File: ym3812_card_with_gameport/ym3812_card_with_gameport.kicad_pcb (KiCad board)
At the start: 2 copper layers, 115.6 x 106.7 mm, 79 parts, among them IC1 74LS138, IC11 NE558, IC12 74HCT02, IC13 74LS74, IC18 74LS244, IC2 74LS138, IC3 74LS138, IC4 74LS245, IC6 YM3812, IC7 Y3014B, IC8 LM324, IC9 TDA7233, J1 Bus_ISA_8bit, J2 Conn_02x04_Odd_Even, J3 Conn_02x03_Counter_Clockwise

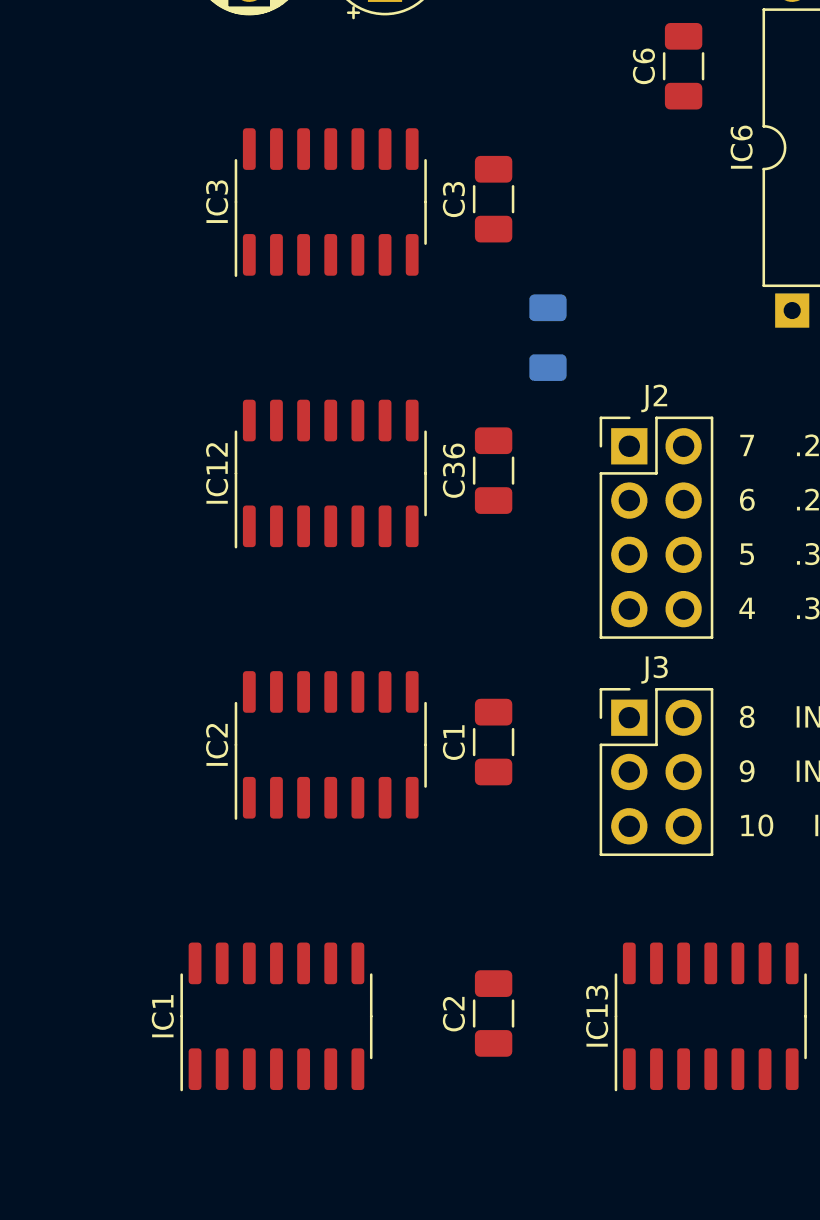
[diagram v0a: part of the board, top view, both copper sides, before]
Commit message: some corrections, GND and VCC
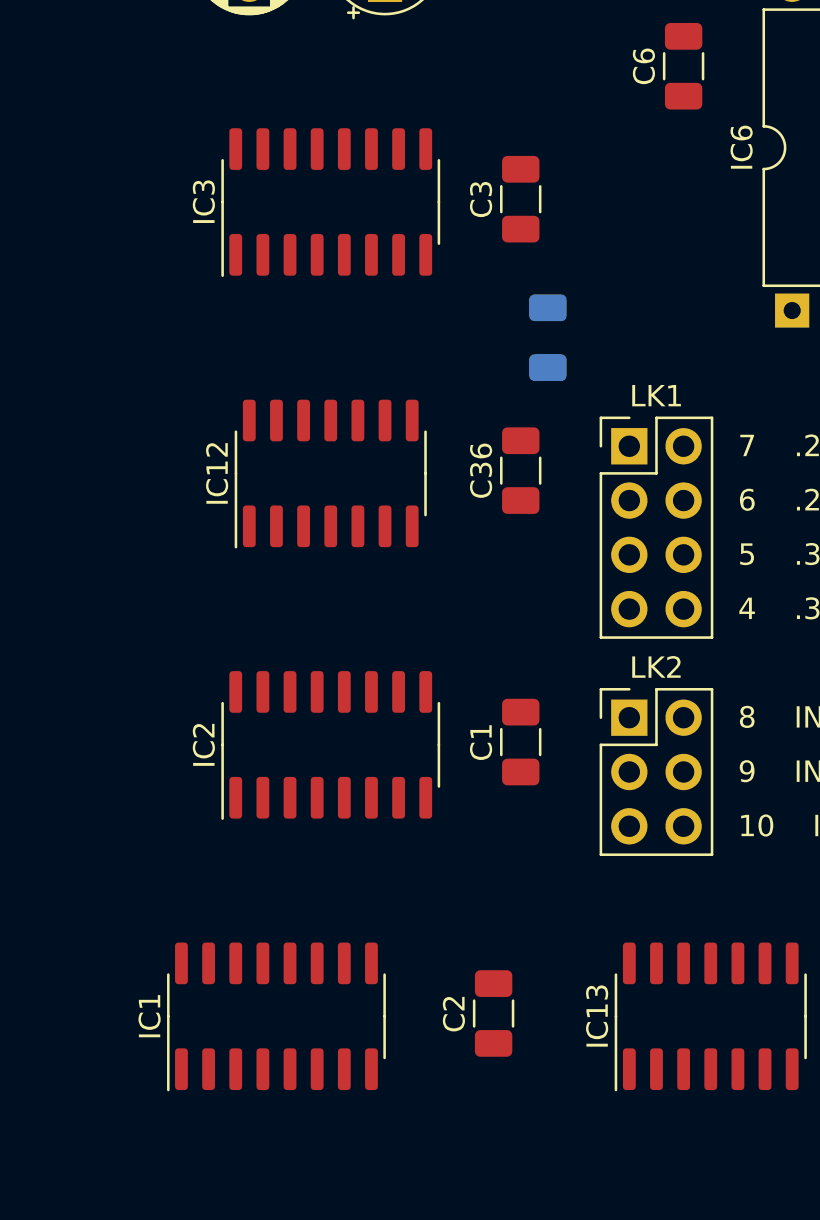
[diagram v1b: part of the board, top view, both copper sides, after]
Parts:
- IC1, IC2, IC3: footprint Package_SO:SOIC-14_3.9x8.7mm_P1.27mm -> Package_SO:SOIC-16_3.9x9.9mm_P1.27mm
- moved C1 1.27 mm to (167.6, 106.5)
- moved C3 1.27 mm to (167.6, 81.2)
- moved C36 1.27 mm to (167.6, 93.8)
- renumbered J2 to LK1, J3 to LK2
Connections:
- C1 pad 1: Net-(C1-Pad1) -> GND
- C1 pad 2: Net-(C1-Pad2) -> +5V
- C10 pad 1: Net-(C10-Pad1) -> GND
- C14 pad 2: Net-(C14-Pad2) -> GND
- C2 pad 1: Net-(C2-Pad1) -> GND
- C2 pad 2: Net-(C2-Pad2) -> +5V
- C20 pad 1: Net-(C20-Pad1) -> GND
- C21 pad 1: Net-(C21-Pad1) -> GND
- C22 pad 2: Net-(C22-Pad2) -> GND
- C23 pad 1: Net-(C23-Pad1) -> GND
- C24 pad 2: Net-(C24-Pad2) -> GND
- C25 pad 2: Net-(C25-Pad2) -> GND
- C26 pad 1: Net-(C26-Pad1) -> GND
- C27 pad 2: Net-(C27-Pad2) -> GND
- C28 pad 1: Net-(C28-Pad1) -> GND
- C3 pad 1: Net-(C3-Pad1) -> GND
- C3 pad 2: Net-(C3-Pad2) -> +5V
- C30 pad 1: Net-(C30-Pad1) -> GND
- C31 pad 1: Net-(C31-Pad1) -> GND
- C32 pad 2: Net-(C32-Pad2) -> GND
- C33 pad 2: Net-(C33-Pad2) -> GND
- C35 pad 2: Net-(C35-Pad2) -> GND
- C36 pad 1: Net-(C36-Pad1) -> GND
- C36 pad 2: Net-(C36-Pad2) -> +5V
- C37 pad 2: Net-(C37-Pad2) -> GND
- C4 pad 1: Net-(C4-Pad1) -> GND
- C4 pad 2: Net-(C4-Pad2) -> +5V
- C6 pad 1: Net-(C6-Pad1) -> +5V
- C6 pad 2: Net-(C6-Pad2) -> GND
- C7 pad 1: Net-(C7-Pad1) -> +5V
- C7 pad 2: Net-(C7-Pad2) -> GND
- C9 pad 2: Net-(C9-Pad2) -> GND
- IC12 pad 14: VCC -> +5V
- IC13 pad 14: Net-(IC13-Pad14) -> +5V
- IC13 pad 7: Net-(IC13-Pad7) -> GND
- IC18 pad 20: VCC -> +5V
- IC4 pad 20: VCC -> +5V
- IC8 pad 11: Net-(IC8-Pad11) -> GND
- IC8 pad 4: Net-(IC8-Pad4) -> +5V
- J1 pad 1: Net-(J1-Pad1) -> GND
- J1 pad 10: Net-(J1-Pad10) -> GND
- J1 pad 29: Net-(J1-Pad29) -> +5V
- J1 pad 3: Net-(J1-Pad3) -> +5V
- J1 pad 31: Net-(J1-Pad31) -> GND
- LK1 pad 2: Net-(J2-Pad2) -> Net-(LK1-Pad2)
- LK1 pad 4: Net-(J2-Pad4) -> Net-(LK1-Pad2)
- LK1 pad 6: Net-(J2-Pad6) -> Net-(LK1-Pad2)
- LK1 pad 8: Net-(J2-Pad8) -> Net-(LK1-Pad2)
- R12 pad 1: Net-(R12-Pad1) -> GND
- R9 pad 1: Net-(R9-Pad1) -> GND
- RV1 pad 3: Net-(RV1-Pad3) -> GND
- SK1 pad S: Net-(SK1-PadS) -> GND
- SK2 pad 1: Net-(SK2-Pad1) -> +5V
- SK2 pad 12: Net-(SK2-Pad12) -> GND
- SK2 pad 15: Net-(SK2-Pad15) -> +5V
- SK2 pad 4: Net-(SK2-Pad4) -> GND
- SK2 pad 5: Net-(SK2-Pad5) -> GND
- SK2 pad 8: Net-(SK2-Pad8) -> +5V
- SK2 pad 9: Net-(SK2-Pad9) -> +5V

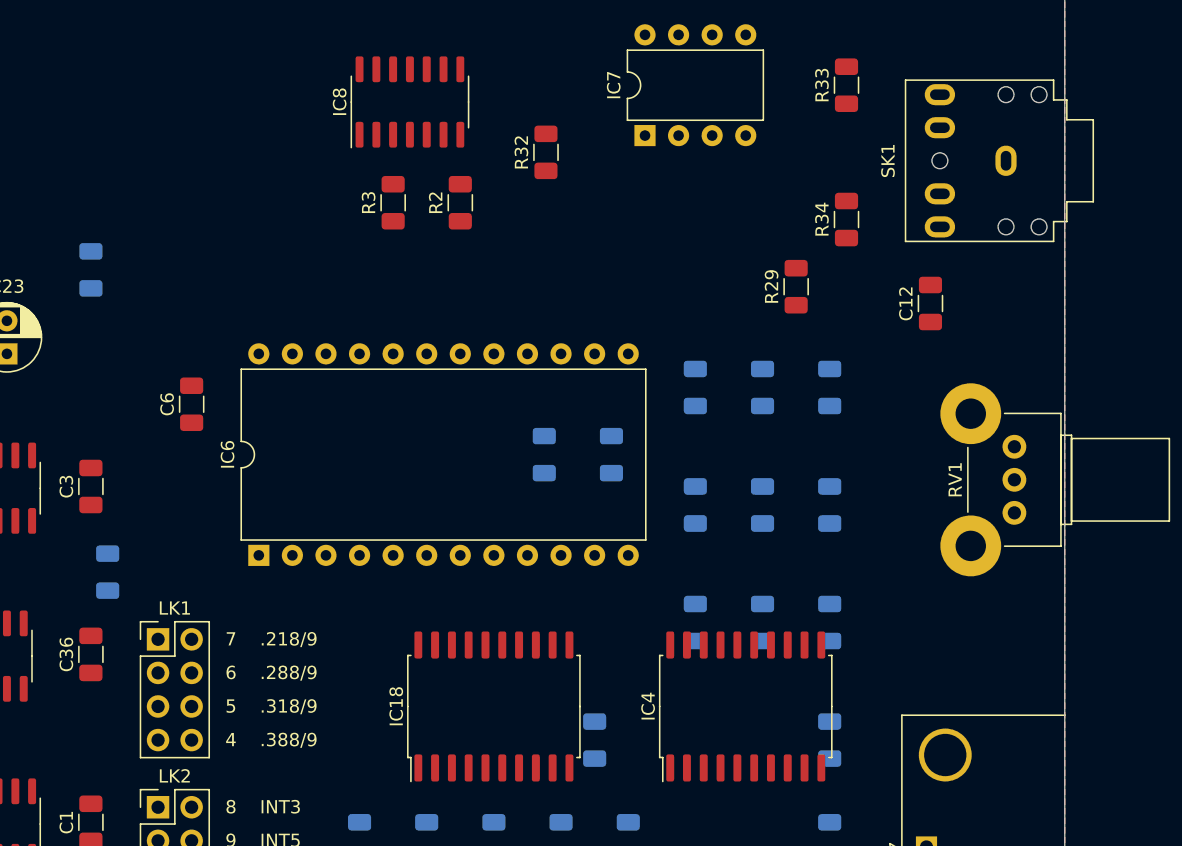
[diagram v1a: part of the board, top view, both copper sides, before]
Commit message: mostly complete schematic
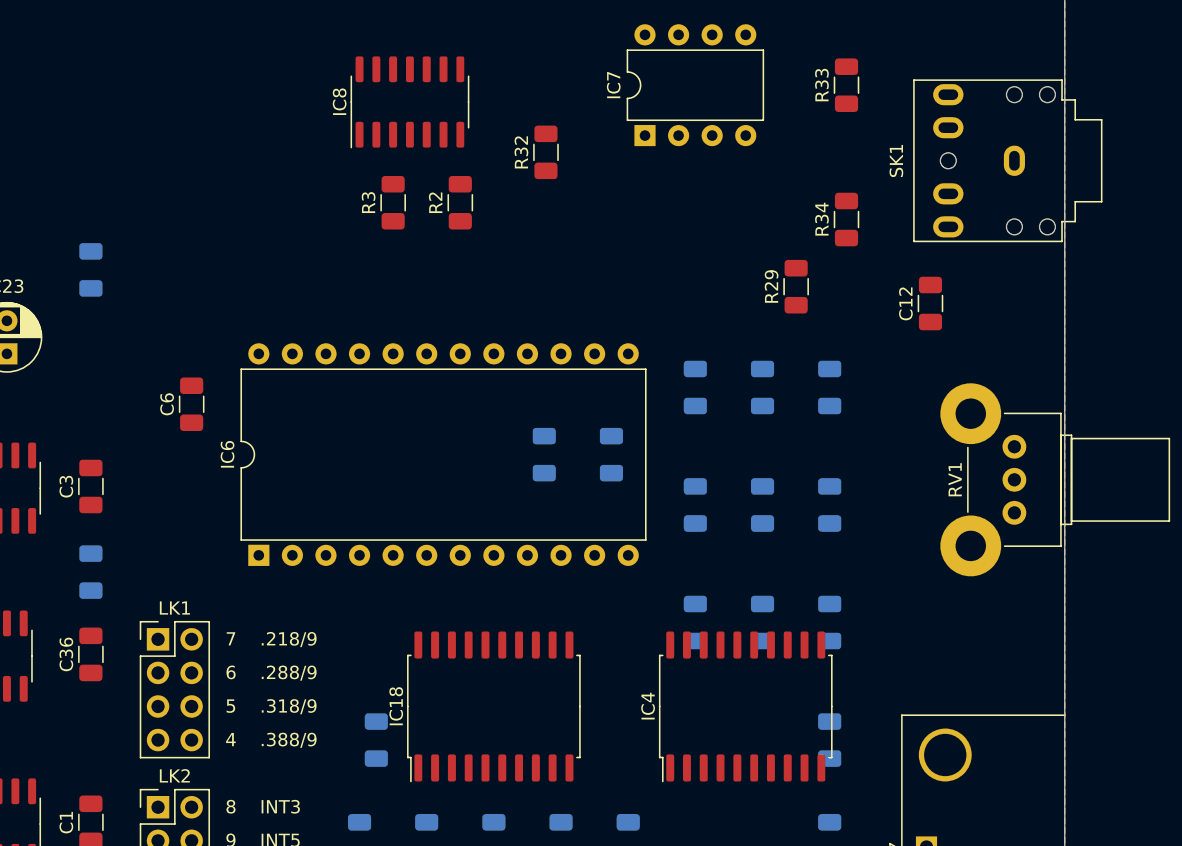
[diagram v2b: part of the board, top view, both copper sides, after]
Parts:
- C21, C34, C37: value C -> 47nF
- LK2: value Conn_02x03_Counter_Clockwise -> Conn_02x03_Odd_Even
- R1: value 22Ω -> 8.2kΩ
- moved C24 16.5 mm to (189.2, 100.3)
- moved R1 1.27 mm to (167.6, 87.6)
- moved SK1 0.64 mm to (237.5, 56.5)
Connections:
- C11 pad 2: Net-(C11-Pad2) -> /AUDIO_OUT
- C13 pad 2: Net-(C13-Pad2) -> +5V
- C20 pad 2: Net-(C20-Pad2) -> +12V
- C21 pad 2: Net-(C21-Pad2) -> -12V
- C22 pad 1: Net-(C22-Pad1) -> +12V
- C23 pad 2: Net-(C23-Pad2) -> -12V
- C24 pad 1: Net-(C24-Pad1) -> +5V
- C25 pad 1: Net-(C25-Pad1) -> /VCTL
- C26 pad 2: Net-(C26-Pad2) -> /BTN2
- C27 pad 1: Net-(C27-Pad1) -> /BTN3
- C28 pad 2: Net-(C28-Pad2) -> /BTN4
- C29 pad 1: Net-(C29-Pad1) -> /BTN1
- C29 pad 2: Net-(C29-Pad2) -> GND
- C30 pad 2: Net-(C30-Pad2) -> /TIMING_D
- C31 pad 2: Net-(C31-Pad2) -> /TIMING_C
- C32 pad 1: Net-(C32-Pad1) -> /TIMING_B
- C33 pad 1: Net-(C33-Pad1) -> /TIMING_A
- C34 pad 1: Net-(C34-Pad1) -> GND
- C34 pad 2: Net-(C34-Pad2) -> +5V
- C35 pad 1: Net-(C35-Pad1) -> +12V
- C37 pad 1: Net-(C37-Pad1) -> +5V
- C5 pad 1: Net-(C5-Pad1) -> +5V
- C5 pad 2: Net-(C5-Pad2) -> GND
- C8 pad 1: Net-(C8-Pad1) -> /PREAMP_OUT
- C8 pad 2: Net-(C8-Pad2) -> /VIN
- IC1 pad 1: Net-(IC1-Pad1) -> /BA01_NOR_BA02
- IC1 pad 12: Net-(IC1-Pad12) -> /MAYBE_OPL
- IC1 pad 14: Net-(IC1-Pad14) -> /MAYBE_JOYSTICK
- IC1 pad 2: Net-(IC1-Pad2) -> /BA03
- IC1 pad 3: Net-(IC1-Pad3) -> /BA05
- IC1 pad 4: Net-(IC1-Pad4) -> /BA06
- IC1 pad 5: Net-(IC1-Pad5) -> /AEN
- IC1 pad 6: Net-(IC1-Pad6) -> /BA09
- IC11 pad 1: Net-(IC11-Pad1) -> /QA
- IC11 pad 10: Net-(IC11-Pad10) -> /TIMING_C
- IC11 pad 11: Net-(IC11-Pad11) -> /JOY_TR
- IC11 pad 12: Net-(IC11-Pad12) -> GND
- IC11 pad 13: Net-(IC11-Pad13) -> +5V
- IC11 pad 14: Net-(IC11-Pad14) -> /JOY_TR
- IC11 pad 15: Net-(IC11-Pad15) -> /TIMING_D
- IC11 pad 16: Net-(IC11-Pad16) -> /QD
- IC11 pad 2: Net-(IC11-Pad2) -> /TIMING_A
- IC11 pad 3: Net-(IC11-Pad3) -> /JOY_TR
- IC11 pad 4: Net-(IC11-Pad4) -> /VCTL
- IC11 pad 5: Net-(IC11-Pad5) -> +5V
- IC11 pad 6: Net-(IC11-Pad6) -> /JOY_TR
- IC11 pad 7: Net-(IC11-Pad7) -> /TIMING_B
- IC11 pad 8: Net-(IC11-Pad8) -> /QB
- IC11 pad 9: Net-(IC11-Pad9) -> /QC
- IC12 pad 1: Net-(IC12-Pad1) -> /BA04_NOR_BA07
- IC12 pad 10: Net-(IC12-Pad10) -> /OPL_IC
- IC12 pad 11: Net-(IC12-Pad11) -> /BA02
- IC12 pad 12: Net-(IC12-Pad12) -> /BA01
- IC12 pad 13: Net-(IC12-Pad13) -> /BA01_NOR_BA02
- IC12 pad 2: Net-(IC12-Pad2) -> /BA07
- IC12 pad 3: Net-(IC12-Pad3) -> /BA04
- IC12 pad 4: Net-(IC12-Pad4) -> /IRQ
- IC12 pad 5: Net-(IC12-Pad5) -> /OPL_IRQ
- IC12 pad 6: Net-(IC12-Pad6) -> /OPL_IRQ
- IC12 pad 8: Net-(IC12-Pad8) -> /RESET
- IC12 pad 9: Net-(IC12-Pad9) -> /RESET
- IC13 pad 1: Net-(IC13-Pad1) -> +5V
- IC13 pad 10: Net-(IC13-Pad10) -> +5V
- IC13 pad 11: Net-(IC13-Pad11) -> /OSC
- IC13 pad 13: Net-(IC13-Pad13) -> +5V
- IC13 pad 4: Net-(IC13-Pad4) -> +5V
- IC13 pad 5: Net-(IC13-Pad5) -> /OPL_CLK
- IC13 pad 6: Net-(IC13-Pad6) -> Net-(IC13-Pad2)
- IC13 pad 8: Net-(IC13-Pad8) -> Net-(IC13-Pad12)
- IC13 pad 9: Net-(IC13-Pad9) -> Net-(IC13-Pad3)
- IC18 pad 1: Net-(IC18-Pad1) -> /JOY_OE
- IC18 pad 11: Net-(IC18-Pad11) -> /BTN4
- IC18 pad 12: Net-(IC18-Pad12) -> /DB3
- IC18 pad 13: Net-(IC18-Pad13) -> /BTN3
- IC18 pad 14: Net-(IC18-Pad14) -> /DB2
- IC18 pad 15: Net-(IC18-Pad15) -> /BTN2
- IC18 pad 16: Net-(IC18-Pad16) -> /DB1
- IC18 pad 17: Net-(IC18-Pad17) -> /BTN1
- IC18 pad 18: Net-(IC18-Pad18) -> /DB0
- IC18 pad 19: Net-(IC18-Pad19) -> /JOY_OE
- IC18 pad 2: Net-(IC18-Pad2) -> /QA
- IC18 pad 3: Net-(IC18-Pad3) -> /DB4
- IC18 pad 4: Net-(IC18-Pad4) -> /QB
- IC18 pad 5: Net-(IC18-Pad5) -> /DB5
- IC18 pad 6: Net-(IC18-Pad6) -> /QC
- IC18 pad 7: Net-(IC18-Pad7) -> /DB6
- IC18 pad 8: Net-(IC18-Pad8) -> /QD
- IC18 pad 9: Net-(IC18-Pad9) -> /DB7
- IC2 pad 1: Net-(IC2-Pad1) -> /BA04
- IC2 pad 10: Net-(IC2-Pad10) -> /P31X
- IC2 pad 13: Net-(IC2-Pad13) -> /P28X
- IC2 pad 14: Net-(IC2-Pad14) -> /P21X
- IC2 pad 2: Net-(IC2-Pad2) -> /BA07
- IC2 pad 3: Net-(IC2-Pad3) -> /BA08
- IC2 pad 4: Net-(IC2-Pad4) -> /MAYBE_OPL
- IC2 pad 5: Net-(IC2-Pad5) -> GND
- IC2 pad 6: Net-(IC2-Pad6) -> /BA01_NOR_BA02
- IC2 pad 9: Net-(IC2-Pad9) -> /P38X
- IC3 pad 1: Net-(IC3-Pad1) -> /BA04_NOR_BA07
- IC3 pad 10: Net-(IC3-Pad10) -> /JOY_OE
- IC3 pad 12: Net-(IC3-Pad12) -> /JOY_TR
- IC3 pad 2: Net-(IC3-Pad2) -> /IOR
- IC3 pad 3: Net-(IC3-Pad3) -> /IOW
- IC3 pad 4: Net-(IC3-Pad4) -> /MAYBE_JOYSTICK
- IC3 pad 5: Net-(IC3-Pad5) -> /BA08
- IC3 pad 6: Net-(IC3-Pad6) -> /BA00
- IC4 pad 1: Net-(IC4-Pad1) -> /IOR
- IC4 pad 11: Net-(IC4-Pad11) -> /OPL_D7
- IC4 pad 12: Net-(IC4-Pad12) -> /OPL_D6
- IC4 pad 13: Net-(IC4-Pad13) -> /OPL_D5
- IC4 pad 14: Net-(IC4-Pad14) -> /OPL_D4
- IC4 pad 15: Net-(IC4-Pad15) -> /OPL_D3
- IC4 pad 16: Net-(IC4-Pad16) -> /OPL_D2
- IC4 pad 17: Net-(IC4-Pad17) -> /OPL_D1
- IC4 pad 18: Net-(IC4-Pad18) -> /OPL_D0
- IC4 pad 19: Net-(IC4-Pad19) -> /OPL_CS
- IC4 pad 2: Net-(IC4-Pad2) -> /DB0
- IC4 pad 3: Net-(IC4-Pad3) -> /DB1
- IC4 pad 4: Net-(IC4-Pad4) -> /DB2
- IC4 pad 5: Net-(IC4-Pad5) -> /DB3
- IC4 pad 6: Net-(IC4-Pad6) -> /DB4
- IC4 pad 7: Net-(IC4-Pad7) -> /DB5
- IC4 pad 8: Net-(IC4-Pad8) -> /DB6
- IC4 pad 9: Net-(IC4-Pad9) -> /DB7
- IC6 pad 1: Net-(IC6-Pad1) -> +5V
- IC6 pad 10: Net-(IC6-Pad10) -> /OPL_D0
- IC6 pad 11: Net-(IC6-Pad11) -> /OPL_D1
- IC6 pad 12: Net-(IC6-Pad12) -> GND
- IC6 pad 13: Net-(IC6-Pad13) -> /OPL_D2
- IC6 pad 14: Net-(IC6-Pad14) -> /OPL_D3
- IC6 pad 15: Net-(IC6-Pad15) -> /OPL_D4
- IC6 pad 16: Net-(IC6-Pad16) -> /OPL_D5
- IC6 pad 17: Net-(IC6-Pad17) -> /OPL_D6
- IC6 pad 18: Net-(IC6-Pad18) -> /OPL_D7
- IC6 pad 2: Net-(IC6-Pad2) -> /OPL_IRQ
- IC6 pad 20: Net-(IC6-Pad20) -> /OPL_SH
- IC6 pad 21: Net-(IC6-Pad21) -> /OPL_OUT
- IC6 pad 23: Net-(IC6-Pad23) -> /OPL_SY
- IC6 pad 24: Net-(IC6-Pad24) -> /OPL_CLK
- IC6 pad 3: Net-(IC6-Pad3) -> /OPL_IC
- IC6 pad 4: Net-(IC6-Pad4) -> /BA00
- IC6 pad 5: Net-(IC6-Pad5) -> /IOW
- IC6 pad 6: Net-(IC6-Pad6) -> /IOR
- IC6 pad 7: Net-(IC6-Pad7) -> /OPL_CS
- IC7 pad 1: Net-(IC7-Pad1) -> +5V
- IC7 pad 2: Net-(IC7-Pad2) -> /DAC_OUT
- IC7 pad 3: Net-(IC7-Pad3) -> /OPL_SH
- IC7 pad 4: Net-(IC7-Pad4) -> /OPL_OUT
- IC7 pad 5: Net-(IC7-Pad5) -> /OPL_SY
- IC7 pad 6: Net-(IC7-Pad6) -> GND
- IC7 pad 7: Net-(IC7-Pad7) -> /DAC_REF
- IC7 pad 8: Net-(IC7-Pad8) -> /DAC_MP
- IC8 pad 1: Net-(IC8-Pad1) -> /PREAMP_OUT
- IC8 pad 10: Net-(IC8-Pad10) -> /DAC_REF
- IC8 pad 11: GND -> -12V
- IC8 pad 12: Net-(IC8-Pad12) -> GND
- IC8 pad 13: Net-(IC8-Pad13) -> GND
- IC8 pad 2: Net-(IC8-Pad2) -> Net-(C13-Pad1)
- IC8 pad 3: Net-(IC8-Pad3) -> GND
- IC8 pad 4: +5V -> +12V
- IC8 pad 8: Net-(IC8-Pad8) -> /DAC_MP
- IC8 pad 9: Net-(IC8-Pad9) -> /DAC_MP
- IC9 pad 1: Net-(IC9-Pad1) -> GND
- IC9 pad 2: Net-(IC9-Pad2) -> GND
- IC9 pad 3: Net-(IC9-Pad3) -> +12V
- IC9 pad 4: Net-(IC9-Pad4) -> GND
- IC9 pad 5: Net-(IC9-Pad5) -> Net-(C11-Pad1)
- IC9 pad 6: Net-(IC9-Pad6) -> Net-(C9-Pad1)
- IC9 pad 7: Net-(IC9-Pad7) -> Net-(C14-Pad1)
- IC9 pad 8: Net-(IC9-Pad8) -> /VIN
- J1 pad 13: Net-(J1-Pad13) -> /IOW
- J1 pad 14: Net-(J1-Pad14) -> /IOR
- J1 pad 2: Net-(J1-Pad2) -> /RESET
- J1 pad 23: Net-(J1-Pad23) -> /IRQ5
- J1 pad 25: Net-(J1-Pad25) -> /IRQ3
- J1 pad 30: Net-(J1-Pad30) -> /OSC
- J1 pad 33: Net-(J1-Pad33) -> /DB7
- J1 pad 34: Net-(J1-Pad34) -> /DB6
- J1 pad 35: Net-(J1-Pad35) -> /DB5
- J1 pad 36: Net-(J1-Pad36) -> /DB4
- J1 pad 37: Net-(J1-Pad37) -> /DB3
- J1 pad 38: Net-(J1-Pad38) -> /DB2
- J1 pad 39: Net-(J1-Pad39) -> /DB1
- J1 pad 4: Net-(J1-Pad4) -> /IRQ2
- J1 pad 40: Net-(J1-Pad40) -> /DB0
- J1 pad 42: Net-(J1-Pad42) -> /AEN
- J1 pad 53: Net-(J1-Pad53) -> /BA09
- J1 pad 54: Net-(J1-Pad54) -> /BA08
- J1 pad 55: Net-(J1-Pad55) -> /BA07
- J1 pad 56: Net-(J1-Pad56) -> /BA06
- J1 pad 57: Net-(J1-Pad57) -> /BA05
- J1 pad 58: Net-(J1-Pad58) -> /BA04
- J1 pad 59: Net-(J1-Pad59) -> /BA03
- J1 pad 60: Net-(J1-Pad60) -> /BA02
- J1 pad 61: Net-(J1-Pad61) -> /BA01
- J1 pad 62: Net-(J1-Pad62) -> /BA00
- J1 pad 7: Net-(J1-Pad7) -> -12V
- J1 pad 9: Net-(J1-Pad9) -> +12V
- LK1 pad 1: Net-(LK1-Pad1) -> /P21X
- LK1 pad 2: Net-(LK1-Pad2) -> /OPL_CS
- LK1 pad 3: Net-(LK1-Pad3) -> /P28X
- LK1 pad 4: Net-(LK1-Pad2) -> /OPL_CS
- LK1 pad 5: Net-(LK1-Pad5) -> /P31X
- LK1 pad 6: Net-(LK1-Pad2) -> /OPL_CS
- LK1 pad 7: Net-(LK1-Pad7) -> /P38X
- LK1 pad 8: Net-(LK1-Pad2) -> /OPL_CS
- LK2 pad 1: Net-(LK2-Pad1) -> /IRQ3
- LK2 pad 2: Net-(LK2-Pad2) -> /IRQ
- LK2 pad 3: Net-(LK2-Pad3) -> /IRQ5
- LK2 pad 4: Net-(LK2-Pad4) -> /IRQ
- LK2 pad 5: Net-(LK2-Pad5) -> /IRQ2
- LK2 pad 6: Net-(LK2-Pad6) -> /IRQ
- R1 pad 1: Net-(R1-Pad1) -> +5V
- R1 pad 2: Net-(R1-Pad2) -> /OPL_IRQ
- R10 pad 1: Net-(R10-Pad1) -> Net-(C13-Pad1)
- R10 pad 2: Net-(R10-Pad2) -> +5V
- R11 pad 1: Net-(R11-Pad1) -> /DAC_MP
- R11 pad 2: Net-(R11-Pad2) -> GND
- R12 pad 2: Net-(R12-Pad2) -> /VIN
- R13 pad 1: Net-(R13-Pad1) -> Net-(C10-Pad2)
- R13 pad 2: Net-(R13-Pad2) -> /AUDIO_OUT
- R14 pad 1: Net-(R14-Pad1) -> +5V
- R14 pad 2: Net-(R14-Pad2) -> /BTN2
- R15 pad 1: Net-(R15-Pad1) -> /BTN3
- R15 pad 2: Net-(R15-Pad2) -> +5V
- R16 pad 1: Net-(R16-Pad1) -> +5V
- R16 pad 2: Net-(R16-Pad2) -> /BTN4
- R18 pad 1: Net-(R18-Pad1) -> +5V
- R18 pad 2: Net-(R18-Pad2) -> /QA
- R19 pad 1: Net-(R19-Pad1) -> +5V
- R19 pad 2: Net-(R19-Pad2) -> /QB
- R2 pad 1: Net-(R2-Pad1) -> Net-(IC8-Pad7)
- R2 pad 2: Net-(R2-Pad2) -> Net-(IC8-Pad6)
- R20 pad 1: Net-(R20-Pad1) -> +5V
- R20 pad 2: Net-(R20-Pad2) -> /QC
- R21 pad 1: Net-(R21-Pad1) -> +5V
- R21 pad 2: Net-(R21-Pad2) -> /QD
- R22 pad 1: Net-(R22-Pad1) -> /TIMING_D
- R22 pad 2: Net-(R22-Pad2) -> /JOY1
- R23 pad 1: Net-(R23-Pad1) -> /TIMING_C
- R23 pad 2: Net-(R23-Pad2) -> /JOY2
- R24 pad 1: Net-(R24-Pad1) -> /TIMING_B
- R24 pad 2: Net-(R24-Pad2) -> /JOY3
- R25 pad 1: Net-(R25-Pad1) -> /TIMING_A
- R25 pad 2: Net-(R25-Pad2) -> /JOY4
- R29 pad 1: Net-(R29-Pad1) -> Net-(C12-Pad2)
- R29 pad 2: Net-(R29-Pad2) -> Net-(C13-Pad1)
- R3 pad 1: Net-(R3-Pad1) -> /DAC_OUT
- R3 pad 2: Net-(R3-Pad2) -> Net-(IC8-Pad5)
- R30 pad 1: Net-(R30-Pad1) -> /BTN1
- R30 pad 2: Net-(R30-Pad2) -> +5V
- R32 pad 1: Net-(R32-Pad1) -> GND
- R32 pad 2: Net-(R32-Pad2) -> /AUDIO_OUT
- R33 pad 1: Net-(R33-Pad1) -> /AUDIO_OUT
- R34 pad 2: Net-(R34-Pad2) -> /AUDIO_OUT
- R5 pad 1: Net-(R5-Pad1) -> +5V
- R5 pad 2: Net-(R5-Pad2) -> /JOY2
- R6 pad 1: Net-(R6-Pad1) -> /JOY3
- R6 pad 2: Net-(R6-Pad2) -> +5V
- R7 pad 1: Net-(R7-Pad1) -> /JOY1
- R7 pad 2: Net-(R7-Pad2) -> +5V
- R8 pad 1: Net-(R8-Pad1) -> +5V
- R8 pad 2: Net-(R8-Pad2) -> /JOY4
- R9 pad 2: Net-(R9-Pad2) -> /PREAMP_OUT
- RV1 pad 1: Net-(RV1-Pad1) -> Net-(IC8-Pad7)
- RV1 pad 2: Net-(RV1-Pad2) -> Net-(C12-Pad1)
- SK1 pad R: Net-(SK1-PadR) -> Net-(R34-Pad1)
- SK1 pad T: Net-(SK1-PadT) -> Net-(R33-Pad2)
- SK2 pad 10: Net-(SK2-Pad10) -> /BTN3
- SK2 pad 11: Net-(SK2-Pad11) -> /JOY3
- SK2 pad 13: Net-(SK2-Pad13) -> /JOY4
- SK2 pad 14: Net-(SK2-Pad14) -> /BTN4
- SK2 pad 2: Net-(SK2-Pad2) -> /BTN1
- SK2 pad 3: Net-(SK2-Pad3) -> /JOY1
- SK2 pad 6: Net-(SK2-Pad6) -> /JOY2
- SK2 pad 7: Net-(SK2-Pad7) -> /BTN2

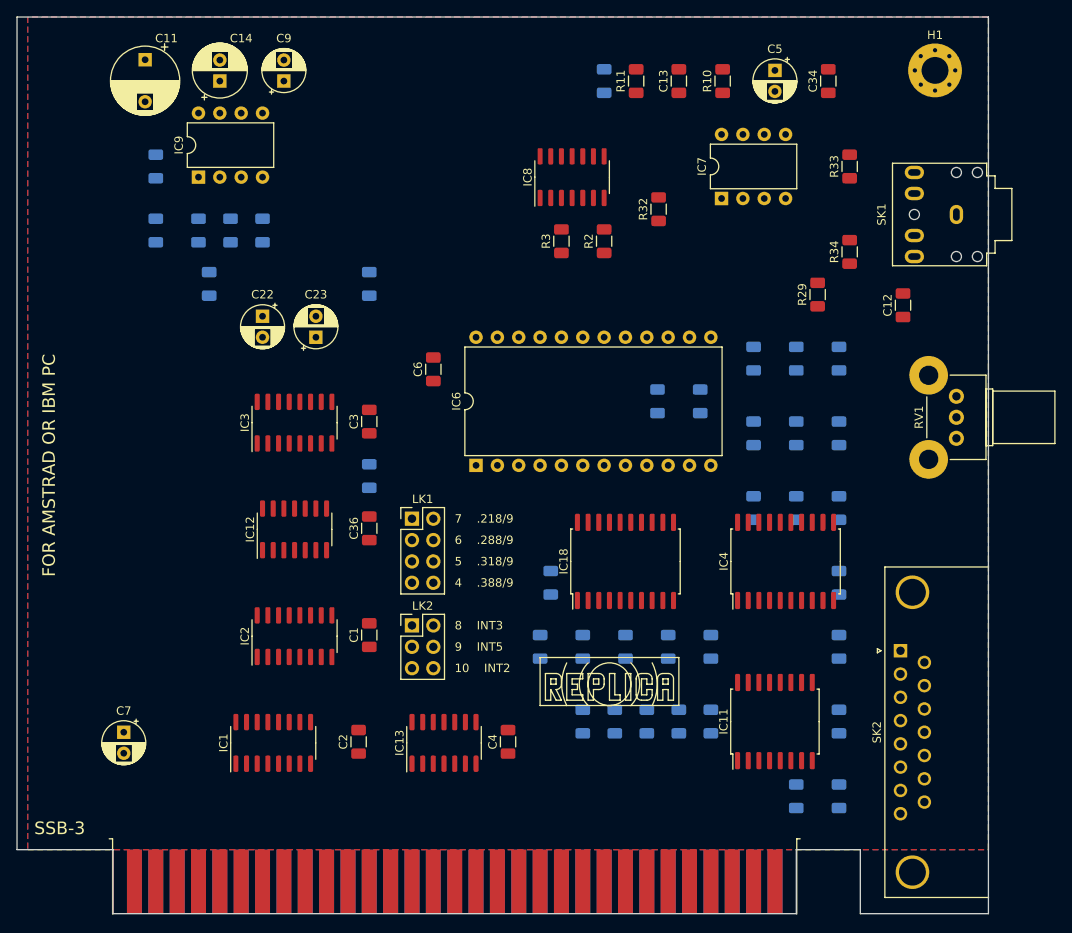
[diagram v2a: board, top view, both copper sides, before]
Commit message: more accurate component positions
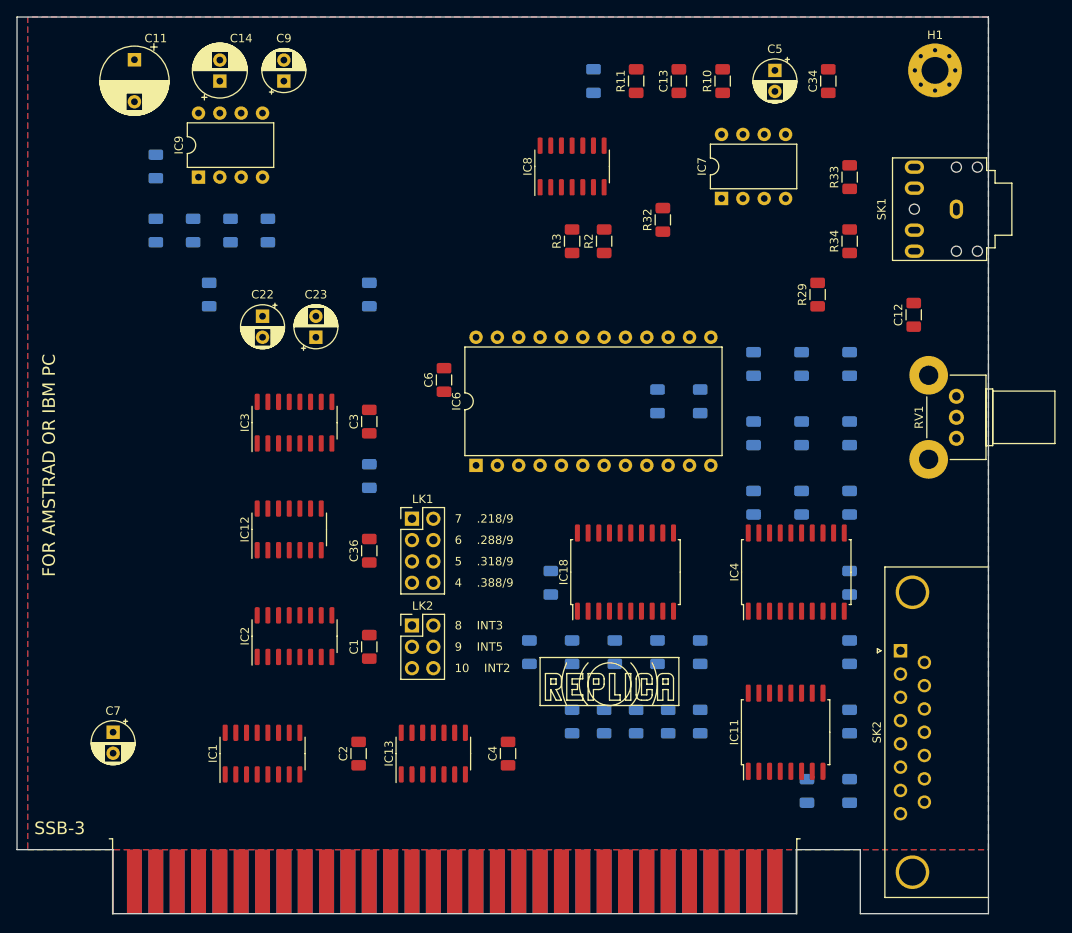
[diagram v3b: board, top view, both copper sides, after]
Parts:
- moved C36 2.67 mm to (167.6, 96.5)
- moved IC1 1.80 mm to (154.9, 120.7)
- moved IC13 1.80 mm to (175.3, 120.7)
- moved C6 1.80 mm to (176.5, 76.2)
- moved IC4 1.80 mm to (218.4, 99.1)
- moved IC11 1.80 mm to (217.2, 118.1)
- moved C12 1.71 mm to (232.4, 68.5)
- moved C25 1.42 mm to (219.7, 125.1)
- moved C28 1.42 mm to (196.8, 108.6)
- moved C29 1.42 mm to (186.7, 108.6)
- moved R21 1.42 mm to (207.0, 108.6)
- moved R25 1.42 mm to (224.8, 125.1)
- moved R7 1.42 mm to (224.8, 74.3)
- moved C26 1.42 mm to (224.8, 90.8)
- moved C27 1.42 mm to (224.8, 108.6)
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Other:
- net class Default: clearance 0.2 -> 0.25; trace_width 0.25 -> 0.3
- net class Power added: clearance 0.25, trace_width 1.2, via_dia 0.8, via_drill 0.4
- rule trace_clearance: 0.2 -> 0.25
